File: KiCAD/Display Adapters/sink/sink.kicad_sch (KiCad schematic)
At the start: 7 parts, among them J1 XT30PW_2_2_-M.G.B, J2 G46M2013201AWEU, J3 20455-040E-76

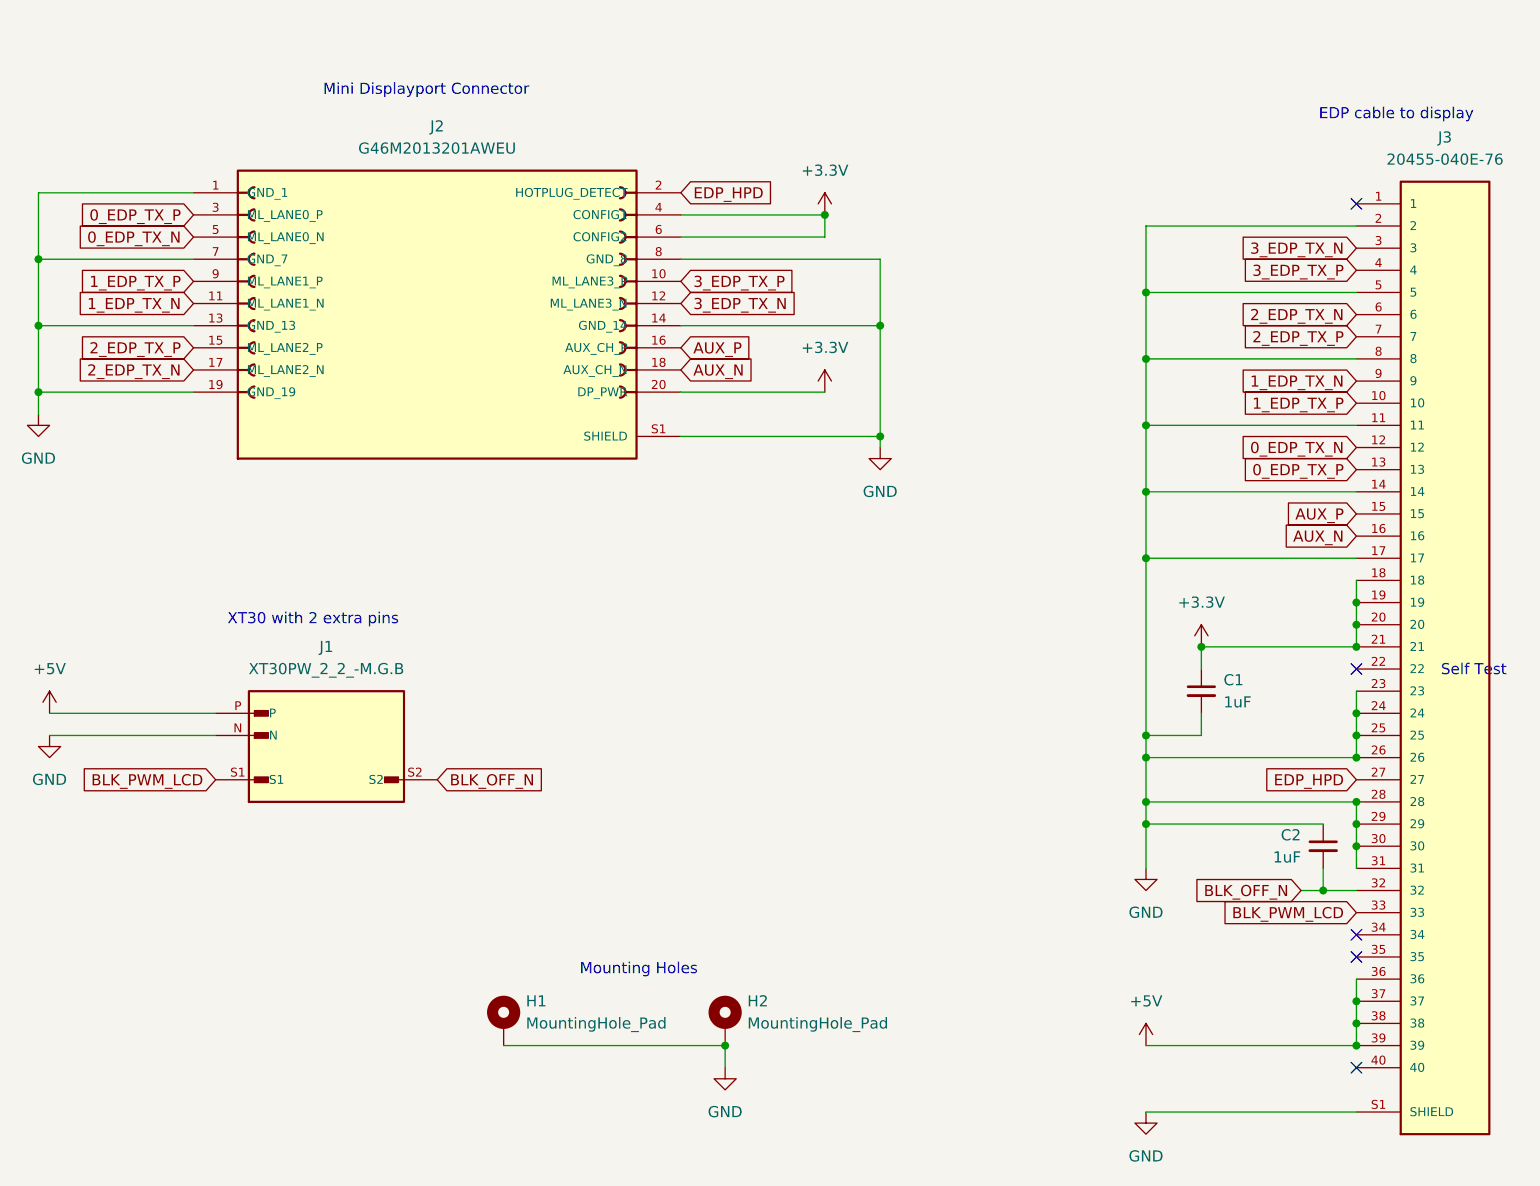
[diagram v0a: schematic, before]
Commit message: use full sized dp instead
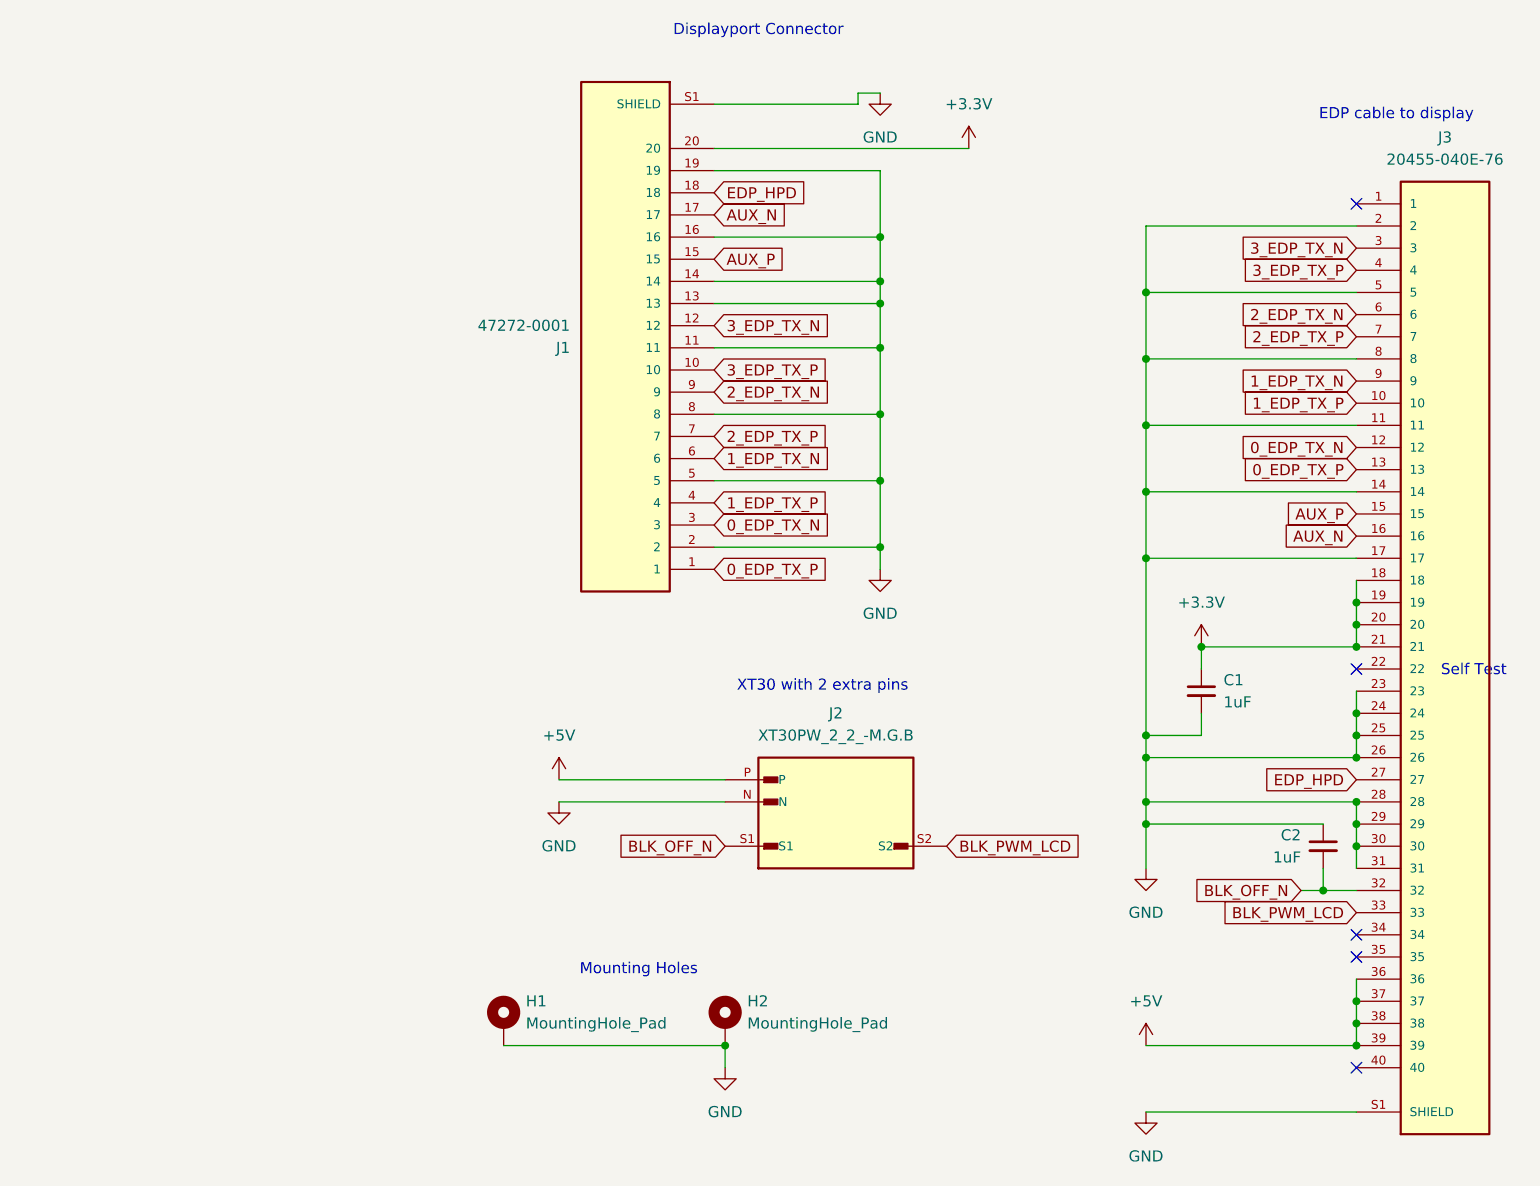
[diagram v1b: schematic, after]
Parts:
- removed J1: XT30PW_2_2_-M.G.B, SnapEDA:AMASS_XT30PW_2_2_-M.G.B, symbol XT30PW_2_2_-M.G.B:XT30PW_2_2_-M.G.B
- removed J2: G46M2013201AWEU, SnapEDA:AMPHENOL_G46M2013201AWEU, symbol G46M2013201AWEU:G46M2013201AWEU
- added J1: 47272-0001, SnapEDA:MOLEX_47272-0001, symbol 47272-0001:47272-0001
- added J2: XT30PW_2_2_-M.G.B, SnapEDA:AMASS_XT30PW_2_2_-M.G.B, symbol XT30PW_2_2_-M.G.B:XT30PW_2_2_-M.G.B
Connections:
- net +3.3V: now also J1.20
- net +5V: now also J2.P
- net 0_EDP_TX_N: now also J1.3
- net 0_EDP_TX_P: now also J1.1
- net 1_EDP_TX_N: now also J1.6
- net 1_EDP_TX_P: now also J1.4
- net 2_EDP_TX_N: now also J1.9
- net 2_EDP_TX_P: now also J1.7
- net 3_EDP_TX_N: now also J1.12
- net 3_EDP_TX_P: now also J1.10
- net AUX_N: now also J1.17
- net AUX_P: now also J1.15
- net BLK_OFF_N: now also J2.S1
- net BLK_PWM_LCD: now also J2.S2
- net EDP_HPD: now also J1.18
- net GND: now also J1.11, J1.13, J1.14, J1.16, J1.19, J1.2, J1.5, J1.8, J1.S1 (SHIELD), J1.S2 (SHIELD), J1.S3 (SHIELD), J1.S4 (SHIELD), J2.N
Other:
- note added: "Displayport Connector"
- note removed: "Mini Displayport Connector"
